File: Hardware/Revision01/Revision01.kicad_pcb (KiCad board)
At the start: 4 copper layers, 100 x 110.1 mm, 100 parts, among them J1 Conn_01x05, J10 StrainConn, J11 StrainConn, J12 StrainConn, J14 Conn_01x05, J2 Conn_01x02, J3 Conn_01x02, J4 Battery connector, J5 StrainConn, J6 StrainConn, J7 StrainConn, J8 StrainConn, J9 StrainConn, Q1 PMOS, Q2 NMOS, Q3 PMOS, SW1 ON/OFF_SW_SPST_LED, U1 NUCLEO-L476RG, U2 MRF89XAM9AT-I/RM, U3 MPU-6500, U5 TPS629203QDRLRQ1

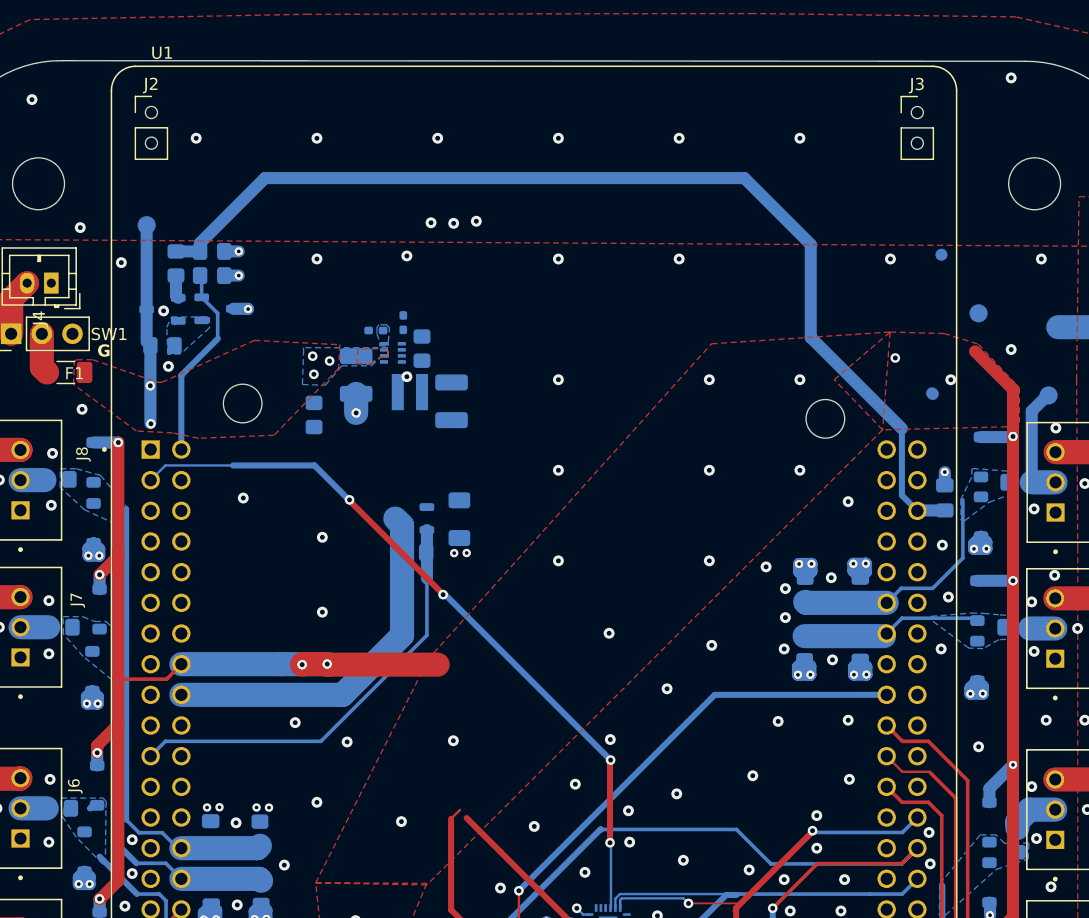
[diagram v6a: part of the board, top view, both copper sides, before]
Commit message: rewired and routed ANOTHER buck converter due to LDO dropout not accounted for.
BATTERY->BUCK_7V ->5V LDO
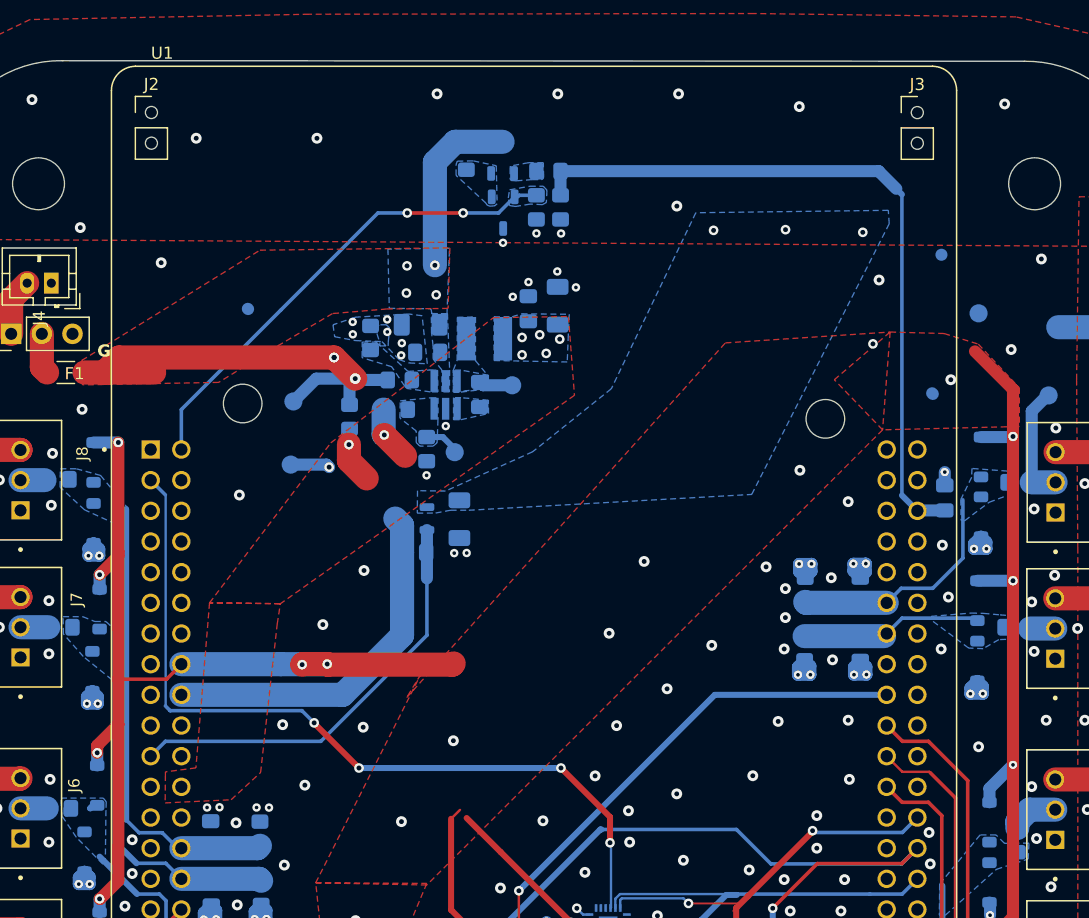
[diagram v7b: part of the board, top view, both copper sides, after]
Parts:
- removed R33: 53.2K, Resistor_SMD:R_0402_1005Metric_Pad0.72x0.64mm_HandSolder
- removed R34: 100K, Resistor_SMD:R_0805_2012Metric_Pad1.20x1.40mm_HandSolder
- removed R35: 124K, Resistor_SMD:R_0402_1005Metric_Pad0.72x0.64mm_HandSolder
- removed U5: TPS629203QDRLRQ1, Package_TO_SOT_SMD:SOT-583-8
- added C22: 1uF, Capacitor_SMD:C_0805_2012Metric_Pad1.18x1.45mm_HandSolder, B.Cu at (159.8, 63.3)
- added C23: 10uF, Capacitor_SMD:C_1206_3216Metric_Pad1.33x1.80mm_HandSolder, B.Cu at (162.2, 63.1)
- added C24: 0.1uF, Capacitor_SMD:C_0805_2012Metric_Pad1.18x1.45mm_HandSolder, B.Cu at (155.8, 70.4)
- added R37: 0, Resistor_SMD:R_0805_2012Metric_Pad1.20x1.40mm_HandSolder, B.Cu at (149.1, 69.2)
- added R38: 0, Resistor_SMD:R_0805_2012Metric_Pad1.20x1.40mm_HandSolder, B.Cu at (146.7, 65.7)
- added R39: 76.8K+- 1%, Resistor_SMD:R_0805_2012Metric_Pad1.20x1.40mm_HandSolder, B.Cu at (148.8, 71.7)
- added R40: 10K +-1%, Resistor_SMD:R_0805_2012Metric_Pad1.20x1.40mm_HandSolder, B.Cu at (151.4, 74.9)
- added TP1: TestPoint, TestPoint:TestPoint_Pad_D1.5mm, B.Cu at (140.1, 76.2)
- added TP2: TestPoint, TestPoint:TestPoint_Pad_D1.5mm, B.Cu at (158.4, 69.6)
- added TP4: TestPoint, TestPoint:TestPoint_Pad_D1.5mm, B.Cu at (140.3, 71.0)
- added U6: LMR51603XFDBVR, LMR51603XFDBVR:DBV0006A-MFG-IPC_A, B.Cu at (152.9, 70.4)
- C20: value 22uF -> 10uF; footprint Capacitor_SMD:C_1210_3225Metric_Pad1.33x2.70mm_HandSolder -> Capacitor_SMD:C_1206_3216Metric_Pad1.33x1.80mm_HandSolder
- C21: value 22uF -> 1uF; footprint Capacitor_SMD:C_1210_3225Metric_Pad1.33x2.70mm_HandSolder -> Capacitor_SMD:C_0805_2012Metric_Pad1.18x1.45mm_HandSolder
- L1: value 2.2uH -> 150uH; footprint VLS3012CX_2R2M_1:IND_VLS3012CX-2R2M-1 -> 74404042151:WE-LQS_4018
- moved R28 31.8 mm to (161.5, 51.9), turned to 180 degrees
- moved TP3 31.7 mm to (153.7, 75.2)
- moved Q3 30.8 mm to (157.7, 50.8), turned to 90 degrees
- moved R27 29.6 mm to (154.7, 50.8), turned to 90 degrees
- moved R29 29.1 mm to (162.5, 54.9), turned to 90 degrees
- moved R26 27.4 mm to (160.5, 54.9), turned to 90 degrees
- moved Q2 25.0 mm to (157.7, 55.3), turned to -90 degrees
- moved L1 7.61 mm to (156.2, 65.8), turned to 180 degrees
- moved C20 6.77 mm to (150.9, 64.6), turned to 180 degrees
- moved C21 4.51 mm to (151.5, 66.9), turned to 180 degrees
- moved R36 2.94 mm to (145.0, 72.3), turned to -90 degrees
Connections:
- C21 pad 1: +Vin_5.5V -> +V_batt
- L1 pad 1: Net-(U5-SW) -> /BuckSW
- L1 pad 2: +Vin_5.5V -> +Vin_7V
- R36 pad 2: +Vin_5.5V -> +Vin_7V
- TP3 pad 1: +V_batt -> /BuckFB
- U1 pad CN7_24: +Vin_5.5V -> +Vin_7V
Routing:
- net /PC5_AIN2_14_BATT_V: track 125.1 -> 60.7 mm
- net +V_batt: track 16.7 -> 57.1 mm, vias 5 -> 7
- net /BatteryV_Div_Enable_GPIO: track 16.3 -> 39.8 mm, vias 0 -> 2
- net +Vin_7V: track 0.00 -> 12.6 mm, vias 0 -> 8
- net /MPU_CS_GPIO: track 61.1 -> 67.5 mm
- net GND: track 105.0 -> 99.8 mm, vias 279 -> 278
- net /BuckFB: track 0.00 -> 2.99 mm
- net /BuckSW: track 0.00 -> 2.80 mm
- net Net-(Q3-D): track 1.93 -> 0.00 mm
- net +3.3V: track 217.3 -> 218.6 mm
- net Net-(Q2-D): track 0.82 -> 0.00 mm
- added copper zone on B.Cu, net (none)
- added copper zone on B.Cu, net +Vin_7V
- added copper zone on F.Cu, net +Vin_7V
- added copper zone on B.Cu, net /Application/+StrainV
- added copper zone on B.Cu, net /BatteryV_Div_Enable_GPIO
- added copper zone on B.Cu, net /BuckEnable
- added copper zone on B.Cu, net /BuckFB
- added copper zone on B.Cu, net /BuckSW
- added copper zone on B.Cu, net Net-(Q3-D)
- added copper zone on B.Cu, net Net-(U6-CB)
- removed copper zone on B.Cu, net Net-(U5-MODE/S-CONF)
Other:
- board text added: "+V_batt"
- board text added: "+Vin7V"
- board text added: "FB"
- board text added: "SW"
